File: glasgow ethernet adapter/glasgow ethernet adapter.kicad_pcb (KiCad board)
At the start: 4 copper layers, 61.7 x 49 mm, 56 parts, among them J1 Glasgow Port, J2 RJ45_Amphenol_RJMG201K21120FR, U1 MxL86110, Y1 25 MHz

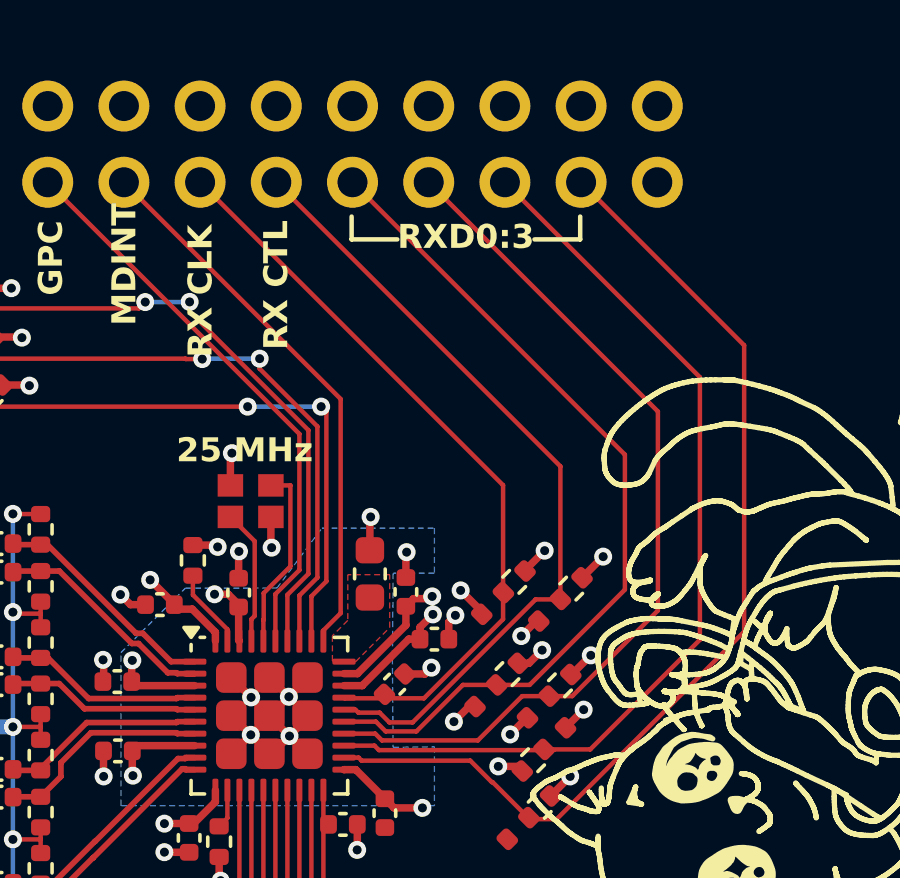
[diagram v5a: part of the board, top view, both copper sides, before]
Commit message: length match RGMII traces
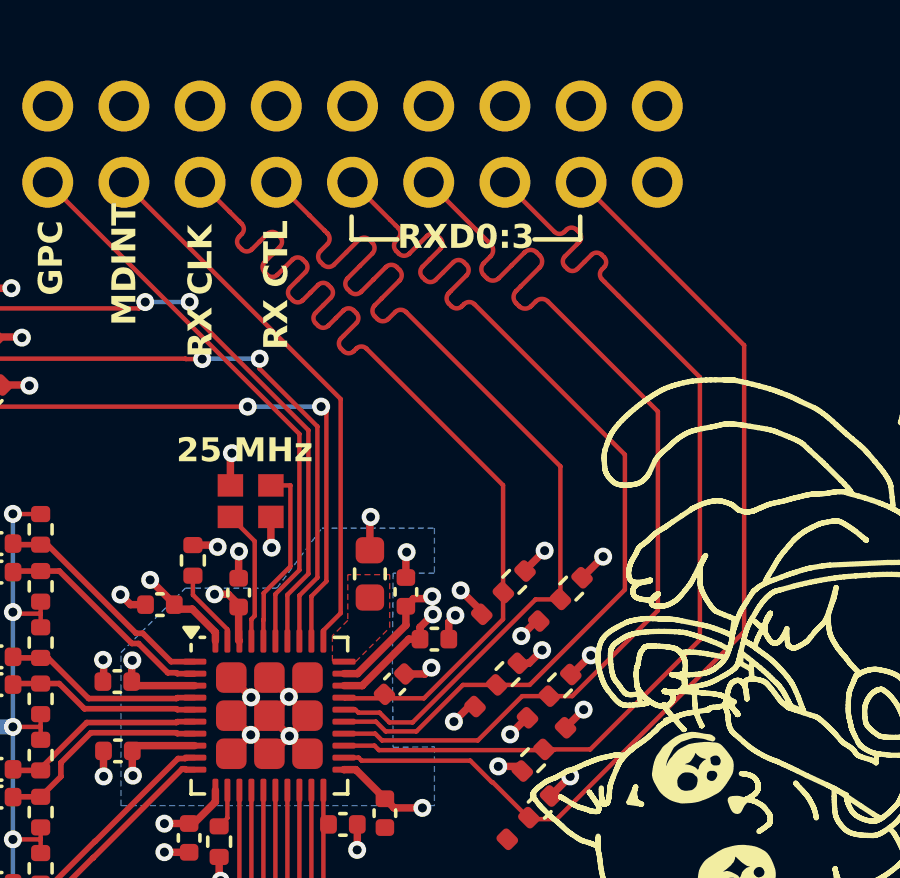
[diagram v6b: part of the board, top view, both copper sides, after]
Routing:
- net /PHYAD1: track 25.2 -> 33.7 mm
- net /PHYAD2: track 26.8 -> 33.7 mm
- net /RXD0: track 28.8 -> 33.9 mm
- net /RXD1: track 29.8 -> 33.9 mm
- net /PLLOFF: track 31.7 -> 34.2 mm

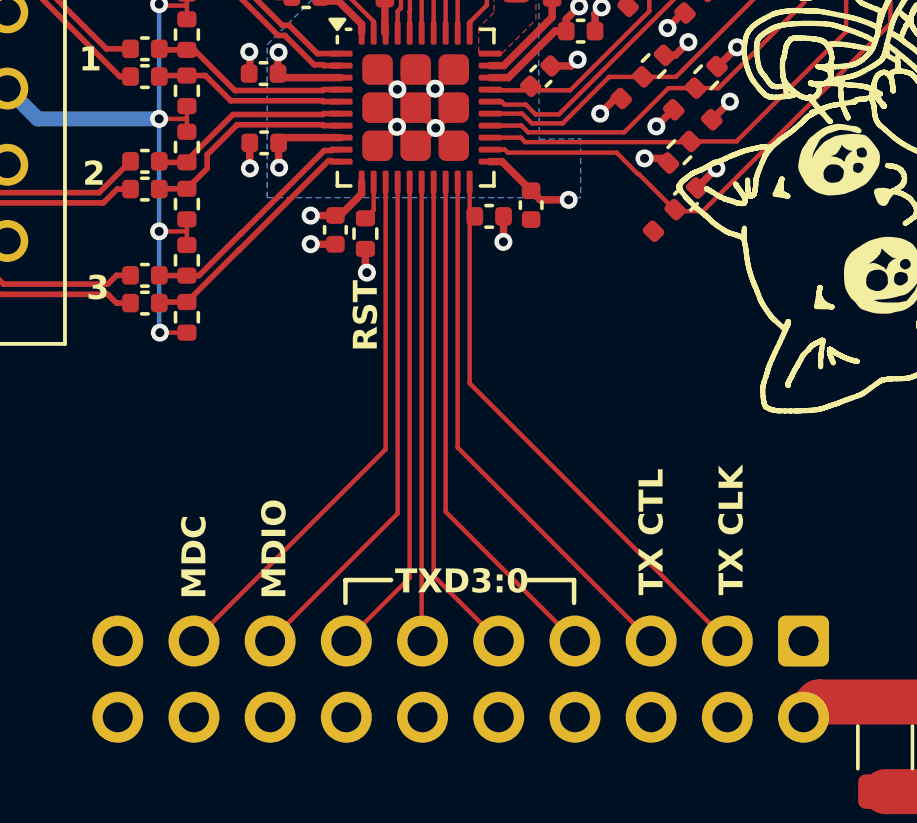
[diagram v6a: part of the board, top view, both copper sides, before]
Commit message: length match RGMII traces
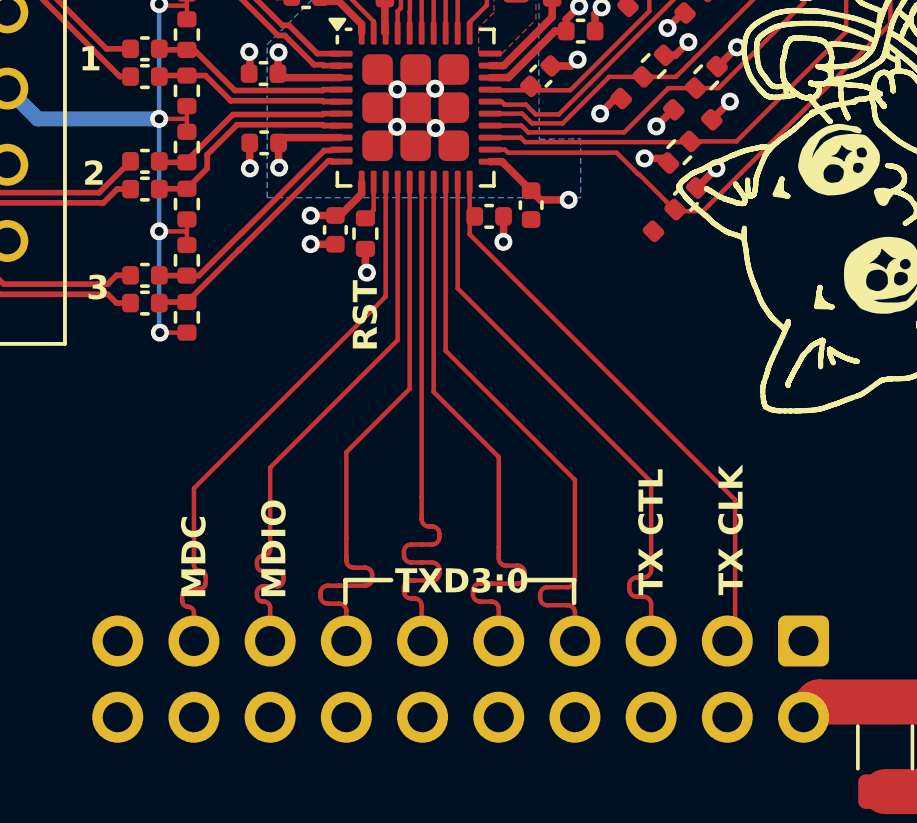
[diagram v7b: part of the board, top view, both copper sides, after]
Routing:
- net /TXD2: track 15.3 -> 18.9 mm
- net /TXD1: track 16.2 -> 19.0 mm
- net /TXD3: track 16.2 -> 18.9 mm
- net /MDIO: track 17.1 -> 18.9 mm
- net /TXD0: track 17.1 -> 18.9 mm
- net /MDC: track 17.9 -> 19.0 mm
- net /TX_CTL: track 18.0 -> 18.9 mm

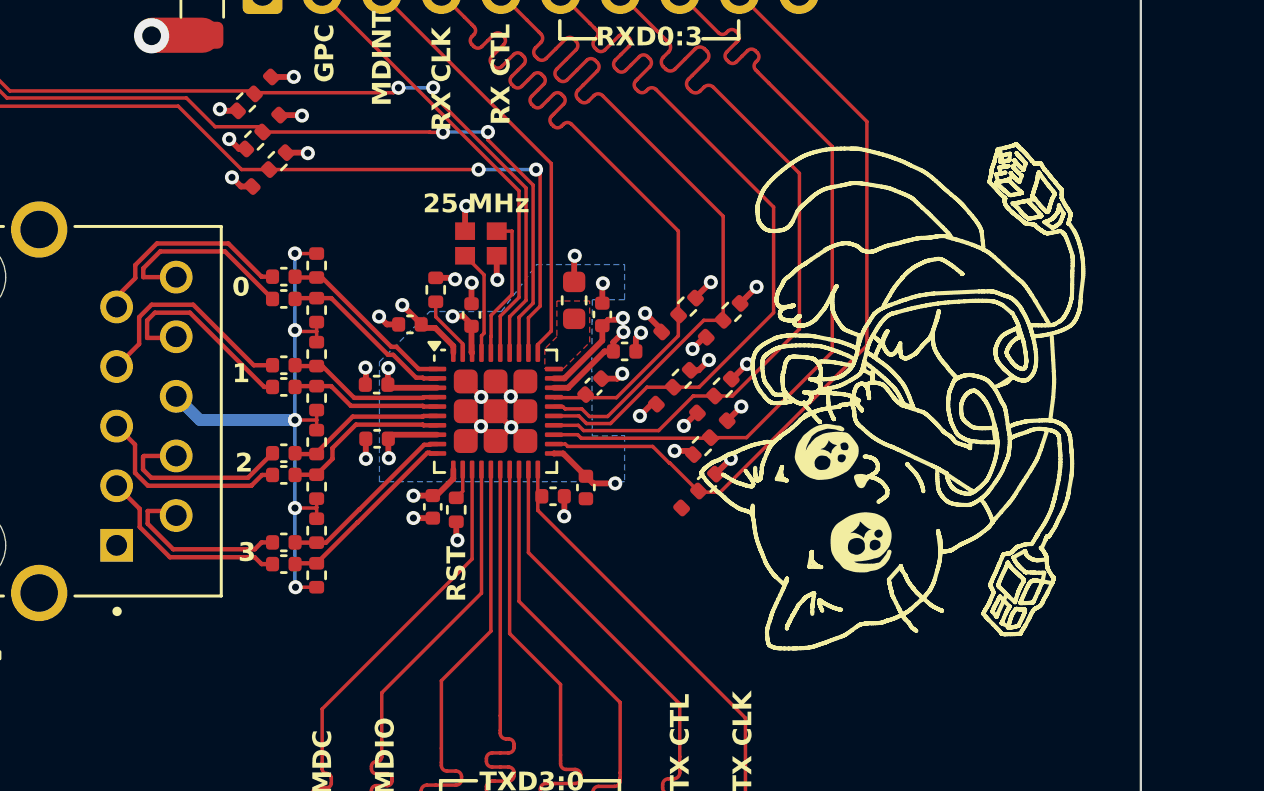
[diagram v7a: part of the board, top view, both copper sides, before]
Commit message: length match diff pairs
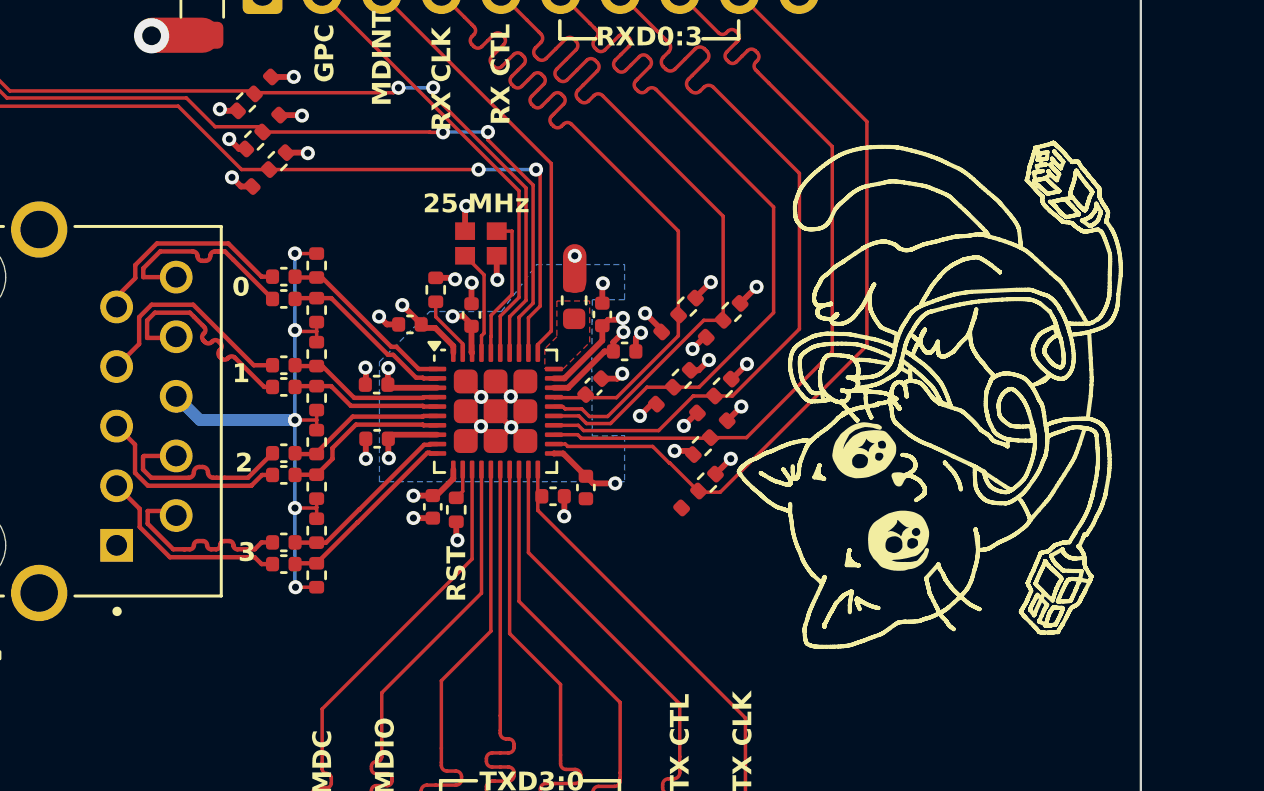
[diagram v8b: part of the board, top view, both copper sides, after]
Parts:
- moved REF** 1.60 mm to (181.8, 99.7)
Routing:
- net /TDX2-: track 8.80 -> 9.78 mm
- net /TDX4+: track 7.73 -> 8.48 mm
